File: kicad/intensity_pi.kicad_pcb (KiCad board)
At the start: 4 copper layers, 62.8 x 172 mm, 126 parts, among them J1 Input A, J2 Input B / Setpoint, J3 Monitor, J4 Output, J7 select 1, J8 Screw_Terminal_01x03, Q1 2N7002E, Q2 2N7002E, SW1 SW_SPDT, SW2 SW_SPDT, SW3 SW_SPDT, SW5 EG6100-ND, U1 LM4040DBZ-5, U10 OPA189, U11 PC817, U12 OPA189, U13 BUF634A, U14 TMUX6123, U17 TMUX6123, U18 OPA189, U19 L7815, U2 LM4040DBZ-5, U20 OPA189, U21 OPA189, U22 4x Comparator, U23 L7915, U3 INA849, U4 INA849, U5 OPA189, U7 OPA189, U8 BUF634A, U9 LM317_TO-252

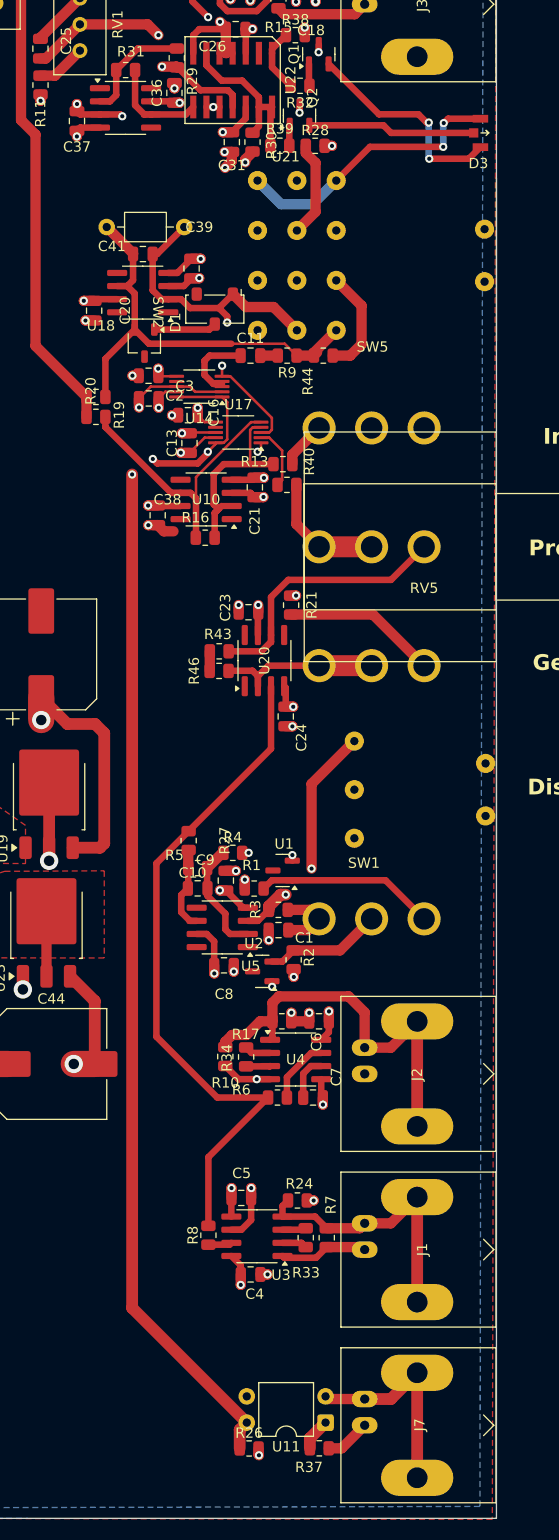
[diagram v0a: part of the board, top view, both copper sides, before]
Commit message: Fixed Digikey Part numbers for some parts, confirmed final BOM, Fixed Switch Footprint hole size
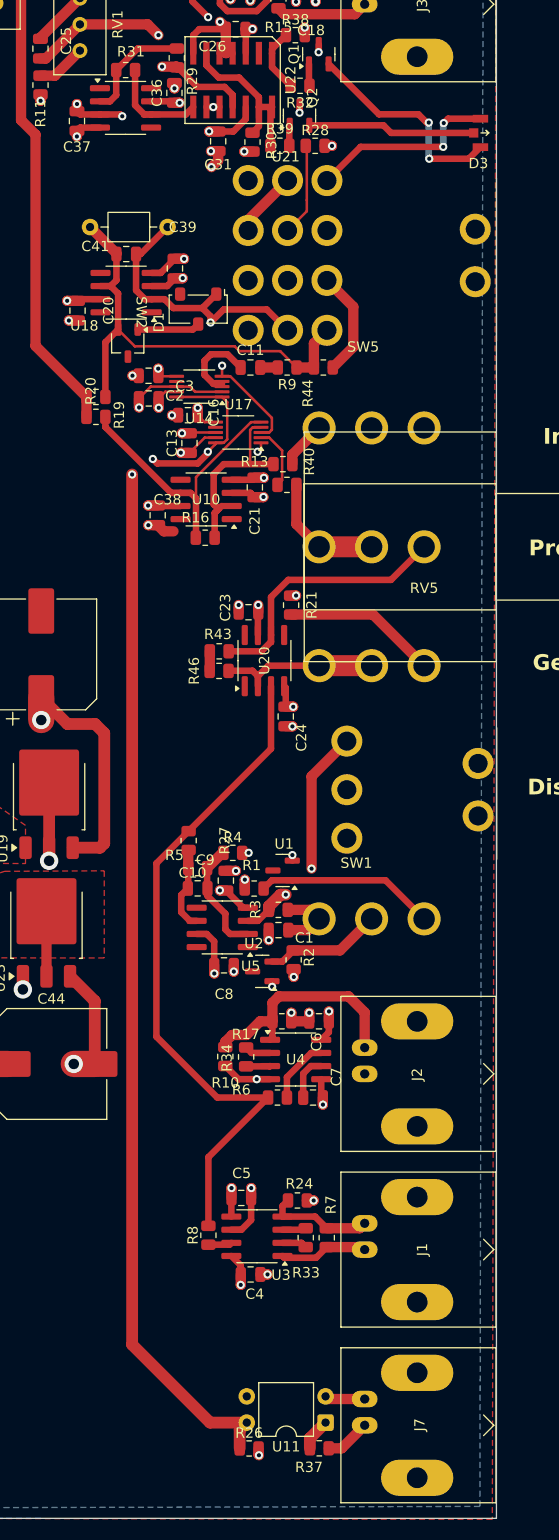
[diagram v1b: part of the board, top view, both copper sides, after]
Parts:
- moved C20 1.61 mm to (-27.8, -37.9)
- moved C41 1.61 mm to (-23.1, -43.3)
- moved C45 1.61 mm to (-19.1, -45.9)
- moved C39 1.61 mm to (-18.4, -41.9)
- moved D1 1.61 mm to (-22.9, -34.7)
- moved SW2 1.61 mm to (-16.1, -38.0)
- moved U18 1.61 mm to (-23.1, -39.6)
- moved C31 1.32 mm to (-14.2, -54.2)
- moved C11 1.15 mm to (-11.1, -32.4)
- moved R44 1.15 mm to (-4.00, -32.4)
- moved R9 1.15 mm to (-7.50, -32.4)
- moved SW5 0.90 mm to (-3.65, -43.2)
- moved SW1 0.73 mm to (-1.73, 8.50)
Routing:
- net Net-(J2-Ext): track 39.1 -> 22.8 mm
- net Net-(J1-Ext): track 26.7 -> 10.4 mm
- net Net-(J7-Ext): track 20.2 -> 3.89 mm
- net Net-(U14C-SEL1): track 124.9 -> 127.0 mm
- net Net-(D1-A): track 42.3 -> 44.1 mm
- net Net-(SW2-A): track 40.3 -> 41.7 mm
- net -15V: track 62.5 -> 63.8 mm
- net Net-(D3-A): track 27.3 -> 28.3 mm
- net Net-(C11-Pad1): track 7.63 -> 8.22 mm
- net +15V: track 74.3 -> 73.7 mm

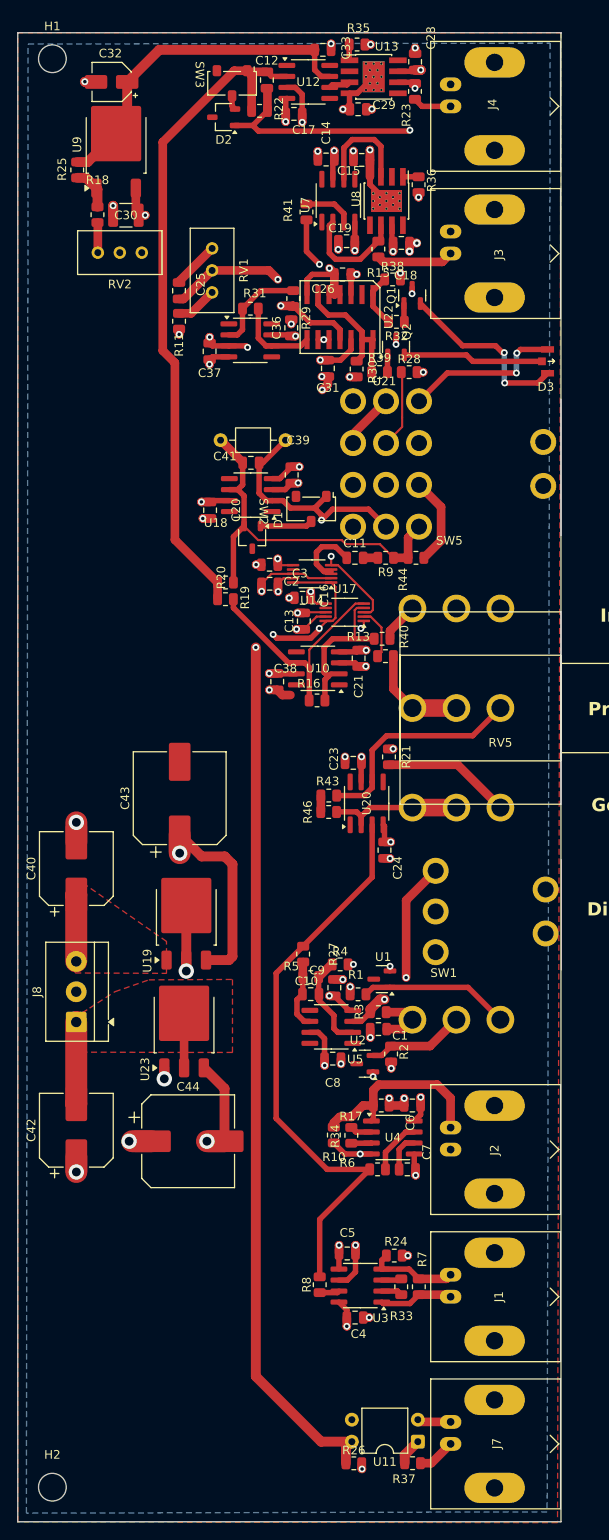
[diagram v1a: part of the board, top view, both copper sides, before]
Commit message: Small Routing Changes, Fix Silkscreen part references
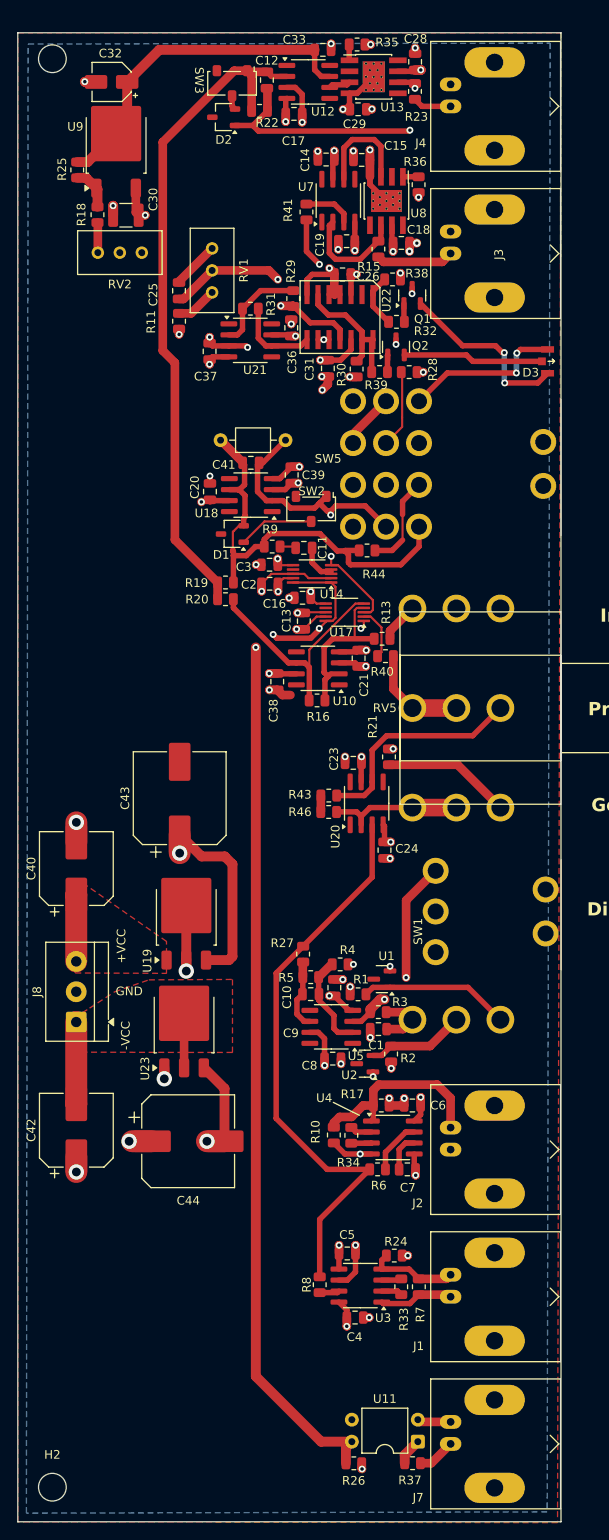
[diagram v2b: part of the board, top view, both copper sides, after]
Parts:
- moved R9 13.2 mm to (-20.6, -33.6), turned to 0 degrees
- moved C11 6.01 mm to (-16.9, -33.5), turned to 180 degrees
- moved R44 5.71 mm to (-9.65, -33.2)
- moved D1 2.33 mm to (-25.2, -35.1), turned to 180 degrees
- moved C20 2.15 mm to (-27.8, -40.0), turned to 90 degrees
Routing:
- net Net-(D1-A): track 44.1 -> 50.3 mm
- net Net-(C11-Pad1): track 8.22 -> 4.83 mm
- net Net-(D1-K): track 6.07 -> 8.79 mm
- net +15V: track 73.7 -> 72.7 mm
- net Net-(R44-Pad1): track 10.3 -> 10.8 mm
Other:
- board text added: "+VCC"
- board text added: "-VCC"
- board text added: "GND"

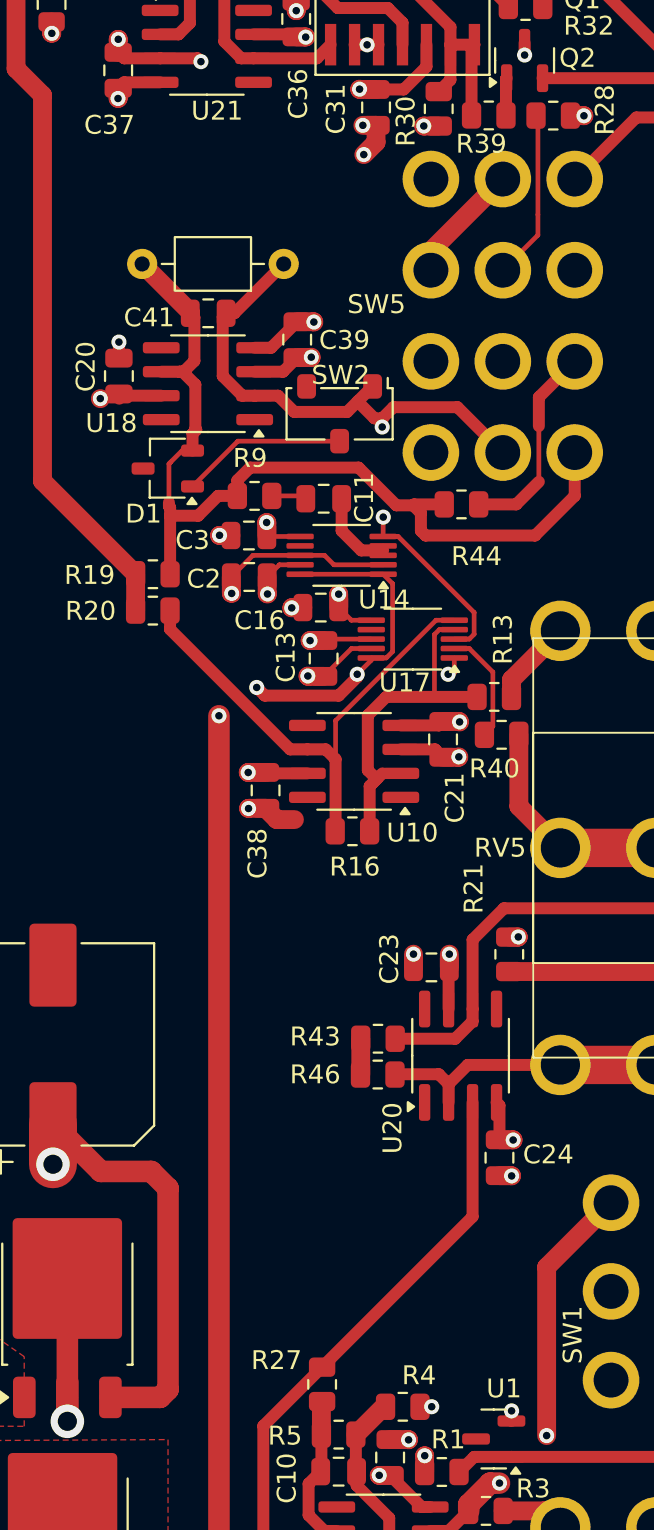
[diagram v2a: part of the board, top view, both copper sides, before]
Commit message: Minor routing improvements
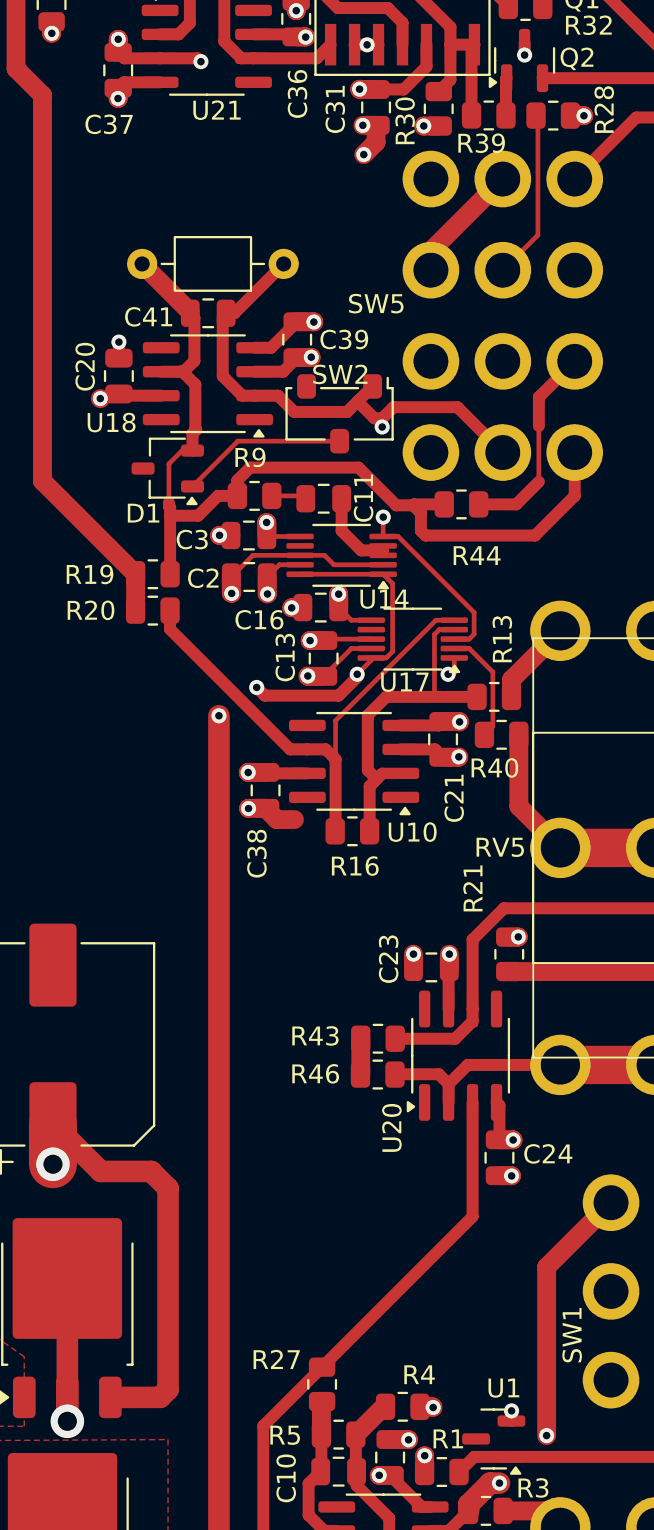
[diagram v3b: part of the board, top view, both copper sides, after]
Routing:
- net GND: track 98.7 -> 99.3 mm
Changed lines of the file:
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@@
 	)
 	(segment
-		(start -16.877054 -26.063274)
-		(end -16.953296 -25.987032)
-		(width 0.25)
-		(layer "F.Cu")
-		(net 2)
-	)
-	(segment
 		(start -40.959423 -87.318069)
 		(end -42.218069 -87.318069)
@@
 	)
 	(segment
+		(start -11.18821 14.61179)
+		(end -11.15 14.65)
+		(width 1)
+		(layer "F.Cu")
+		(net 2)
+	)
+	(segment
 		(start -33.067 26.56)
 		(end -33.067 27.823)
@@
 	)
 	(segment
+		(start -11.847334 14.61179)
+		(end -11.18821 14.61179)
+		(width 1)
+		(layer "F.Cu")
+		(net 2)
+	)
+	(segment
 		(start -4.202874 35.242679)
 		(end -5.216642 35.242679)
@@
 	)
 	(via
-		(at -11.227542 14.608928)
+		(at -11.15 14.65)
 		(size 0.8)
 		(drill 0.4)
@@
 	)
 	(segment
-		(start -16.32063 -15.89959)
-		(end -16.34042 -15.8798)
-		(width 0.635)
-		(layer "F.Cu")
-		(net 8)
-	)
-	(segment
 		(start -25.090664 -26.582717)
 		(end -18.726782 -20.218835)
@@
 	)
 	(segment
-		(start -18.05 -33.65)
-		(end -17.9 -33.5)
-		(width 0.25)
-		(layer "F.Cu")
-		(net 25)
-	)
-	(segment
 		(start -11.969087 -86.987845)
 		(end -11.676509 -87.280423)
@@
 	)
 	(segment
-		(start -19.979041 -18.948835)
-		(end -20.028304 -18.998098)
-		(width 0.635)
-		(layer "F.Cu")
-		(net 43)
-	)
-	(segment
 		(start -31.367141 -58.765882)
 		(end -31.367141 -58.170763)
@@
 	)
 	(segment
-		(start -27.623917 -38.96)
-		(end -27.783456 -38.800461)
-		(width 0.635)
-		(layer "F.Cu")
-		(net 43)
-	)
-	(segment
 		(start -6.778025 -70.772114)
 		(end -6.778025 -68.857153)
@@
 	)
 	(segment
-		(start -19.910521 -31.5)
-		(end -19.962905 -31.552384)
-		(width 0.25)
-		(layer "F.Cu")
-		(net 61)
-	)
-	(segment
 		(start -10.626215 -21.699403)
 		(end -9.775887 -21.699403)
@@
 	)
 	(segment
-		(start -26.915664 -29.496836)
-		(end -26.9125 -29.5)
-		(width 1)
-		(layer "F.Cu")
-		(net 63)
-	)
-	(segment
 		(start -22.984247 -88.108233)
 		(end -23.493357 -88.617343)
@@
 	)
 	(segment
-		(start -24.019243 -43.325933)
-		(end -24.019243 -43.390463)
-		(width 1)
-		(layer "F.Cu")
-		(net 65)
-	)
-	(segment
 		(start -24.37 -40.23)
 		(end -23.8 -40.8)
@@
 	)
 	(segment
-		(start -24.45 -36.05)
-		(end -25.05 -35.45)
+		(start -25.15 -35.35)
+		(end -24.45 -36.05)
 		(width 0.25)
 		(layer "F.Cu")
@@
 	)
 	(segment
-		(start -25.05 -35.45)
-		(end -25.15 -35.35)
-		(width 0.25)
-		(layer "F.Cu")
-		(net 65)
-	)
-	(segment
 		(start -3.65 -35.948)
 		(end -3.65 -33.65)
@@
 	)
 	(segment
-		(start -22.3 -43.145176)
-		(end -22.119243 -43.325933)
-		(width 0.635)
-		(layer "F.Cu")
-		(net 66)
-	)
-	(segment
 		(start -7.46 -35.948)
 		(end -9.862 -38.35)
@@
 	)
 	(segment
-		(start -5.6 -53.7)
-		(end -5.7 -53.8)
-		(width 0.25)
-		(layer "F.Cu")
-		(net 85)
-	)
-	(segment
 		(start -5.6 -47.468)
-		(end -5.6 -48.55)
-		(width 0.25)
-		(layer "F.Cu")
-		(net 85)
-	)
-	(segment
-		(start -5.6 -48.55)
 		(end -5.6 -53.7)
 		(width 0.25)
@@
 		)
 	)
-	(group ""
-		(members "07818761-b36e-4f5e-a901-ee53c1aa8d8c" "09cc3579-fcf3-4942-a920-7498b65e9b41"
-			"0f2973b5-f321-4e51-a9dd-ff96553f5a85" "105b5c29-bfb1-4827-938b-2bfc2c1c4388"
-			"11354248-f3d1-46c7-9c16-c32acd09e103" "11c7ac7a-1cb8-4649-9c78-705f3ef479eb"
-			"296f3ba9-466a-4328-9ef5-b84105489edb" "29d94860-09d5-4aee-8920-b745d931d977"
-			"2abed079-dec1-4467-98d8-48260ab9422f" "4600aa5d-0c18-4f90-978c-57af65270fa9"
-			"575bb3c1-669b-4651-bc9f-d52f1ee1f730" "5ba58dbf-1ffe-4952-9d6b-7396edacb780"
-			"7ba0758a-1054-4525-ba4b-ccc79e7c343c" "803906a9-cf26-4db5-8ea3-28a243bd2b34"
-			"820dab55-0987-431a-9014-9d5a7aa7c4ad" "849d7a56-2b8b-47b0-a072-fff42920cb2e"
-			"8f497584-e60e-407c-aded-cb9d7cda9660" "aab9312d-711b-4449-84f2-04cbce04fd34"
-			"b052c22e-0b00-4ae7-a715-c6b9016e1685" "b8363719-7b07-468a-882e-eb637e79586b"
-			"baf5ea1a-56b3-4f07-b977-7db1a7341f65" "ccb24dae-6639-4078-bc64-48d57670d0d0"
-			"cdc6d46a-7d3f-466d-9941-d634fbf900f1" "cfdb2d6a-90e6-4bb1-bd3b-81e3276980e5"
-			"da71d694-5443-46c5-9701-9dff52398551" "dea7a3e1-a918-4c9d-870c-ab4ed97a29dd"
-			"e0ca3871-40b0-494f-a226-b3e1f99fdf97" "e5c6a181-afde-47d9-9cb3-ea21eeb1eb1f"
-			"e7237a4c-6947-4116-808d-407cf778c114" "e9ad14da-de6e-4075-a457-52acc5af847a"
-			"efa09735-2276-4bf1-a15b-8f3a551c83fd" "f169a570-878c-430e-81f0-33bd60aedd8b"
-			"f4b249c0-21ea-435a-8c30-fd650abee7e6" "f67f4ac5-1183-4cfc-bba6-45b9c8baa503"
-		)
-	)
